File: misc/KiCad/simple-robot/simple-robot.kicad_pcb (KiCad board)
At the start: 2 copper layers, 99.8 x 81 mm, 44 parts, among them J1 MotLA, J10 Screw_Terminal_2_P5.00mm, J2 MotLB, J4 MotRA, J5 MotRB, J6 ENC_LF, J7 ENC_LR, J8 ENC_RF, J9 ENC_RR

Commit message: Update KiCad schematic to include all connections and IC
Make KiCad PCB 4-layer and update footprints
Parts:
- removed D3: LED_RAGB, common-hobby-things:LED RAGB
- removed R2, R3: 330k, Resistor_THT:R_Axial_DIN0207_L6.3mm_D2.5mm_P10.16mm_Horizontal
- added C19: 100nF_Ceramic, Capacitor_THT:C_Disc_D5.0mm_W2.5mm_P2.50mm, F.Cu at (-31.4, 168.1)
- added C20: 100nF_Ceramic, Capacitor_THT:C_Disc_D5.0mm_W2.5mm_P2.50mm, F.Cu at (40.8, 86.7)
- added C21: 100nF_Ceramic, Capacitor_THT:C_Disc_D5.0mm_W2.5mm_P2.50mm, F.Cu at (40.8, 90.8)
- added I1: ~, common-hobby-things:ICM-20948-module, F.Cu at (50.5, 86.8)
- added J11: JST02 HC-SR04, Connector_JST:JST_EH_B2B-EH-A_1x02_P2.50mm_Vertical, F.Cu at (-8.50, 162.2)
- added J3: JST03 Servo, Connector_JST:JST_EH_B3B-EH-A_1x03_P2.50mm_Vertical, F.Cu at (-8.50, 168.0)
- added LED1: LED_5mm_RGB_Kcom_RKGB, PCM_LED_THT_AKL:LED_D5.0mm-4_RGB_Wide_Pins, F.Cu at (88.1, 120.0)
- added R10: 220ohm, Resistor_THT:R_Axial_DIN0207_L6.3mm_D2.5mm_P10.16mm_Horizontal, F.Cu at (-10.4, 145.9)
- added R11: 220ohm, Resistor_THT:R_Axial_DIN0207_L6.3mm_D2.5mm_P10.16mm_Horizontal, F.Cu at (-10.4, 149.9)
- added R7: 20k, Resistor_THT:R_Axial_DIN0207_L6.3mm_D2.5mm_P10.16mm_Horizontal, F.Cu at (148.0, 61.5)
- added R8: 10k, Resistor_THT:R_Axial_DIN0207_L6.3mm_D2.5mm_P10.16mm_Horizontal, F.Cu at (152.3, 64.5)
- added R9: 330ohm, Resistor_THT:R_Axial_DIN0207_L6.3mm_D2.5mm_P10.16mm_Horizontal, F.Cu at (-10.4, 141.8)
- added SW1: RotaryEncoder_Switch, Rotary_Encoder:RotaryEncoder_Alps_EC11E-Switch_Vertical_H20mm, F.Cu at (98.2, 134.1)
- added U1: Pico2, PCM_SL_Development_Boards:raspberry_pi_pico_THT, F.Cu at (87.8, 64.8)
- added U2: CD4049UB, Package_DIP:DIP-16_W7.62mm_LongPads, F.Cu at (29.1, 86.7)
- moved B1 163.2 mm to (135.8, 64.7), turned to 180 degrees
- moved J10 131.5 mm to (147.8, 47.2), turned to 90 degrees
- moved C18 130.0 mm to (146.0, 74.2), turned to -90 degrees
- moved R4 121.3 mm to (152.3, 68.0), turned to 180 degrees
- moved MD1 117.2 mm to (113.1, 93.8), turned to 90 degrees
- moved C7 109.6 mm to (137.0, 70.8), turned to 90 degrees
- moved C1 102.0 mm to (137.2, 87.8), turned to 90 degrees
- moved MD2 98.7 mm to (113.1, 77.3), turned to 90 degrees
- moved R1 96.5 mm to (-80.8, 61.1)
- moved OLED1 93.8 mm to (68.5, 119.3)
- moved LS_1 87.3 mm to (65.1, 52.1)
- moved LS_2 87.0 mm to (79.5, 52.2)
- moved LS_3 86.9 mm to (93.9, 52.2)
- moved R6 25.6 mm to (34.9, 65.0)
- moved R5 16.9 mm to (35.2, 69.8)
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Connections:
- C14 pad 1: +5V -> +3V3
- LS_3 pad 1: unconnected-(LS_3-LV1-Pad1) -> US_SERVO
- LS_3 pad 11: unconnected-(LS_3-HV3-Pad11) -> Net-(LS_3-HV3)
- LS_3 pad 12: unconnected-(LS_3-HV4-Pad12) -> Net-(LS_3-HV4)
- LS_3 pad 3: unconnected-(LS_3-LV-Pad3) -> +3V3
- LS_3 pad 5: unconnected-(LS_3-LV3-Pad5) -> US_ECHO
- LS_3 pad 6: unconnected-(LS_3-LV4-Pad6) -> US_TRIG
- LS_3 pad 7: unconnected-(LS_3-HV1-Pad7) -> Net-(LS_3-HV1)
- LS_3 pad 9: unconnected-(LS_3-HV-Pad9) -> +5V
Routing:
- added copper zone on In2.Cu, net +3V3
- added copper zone on In1.Cu, net GND
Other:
- board size 99.8 x 81 mm -> 100 x 100 mm
- copper layers 2 -> 4
- board text added: "+"
- board text added: "-"
- board text added: "simple-robot 1-rafael-1 rev. 0.4 02/2026"

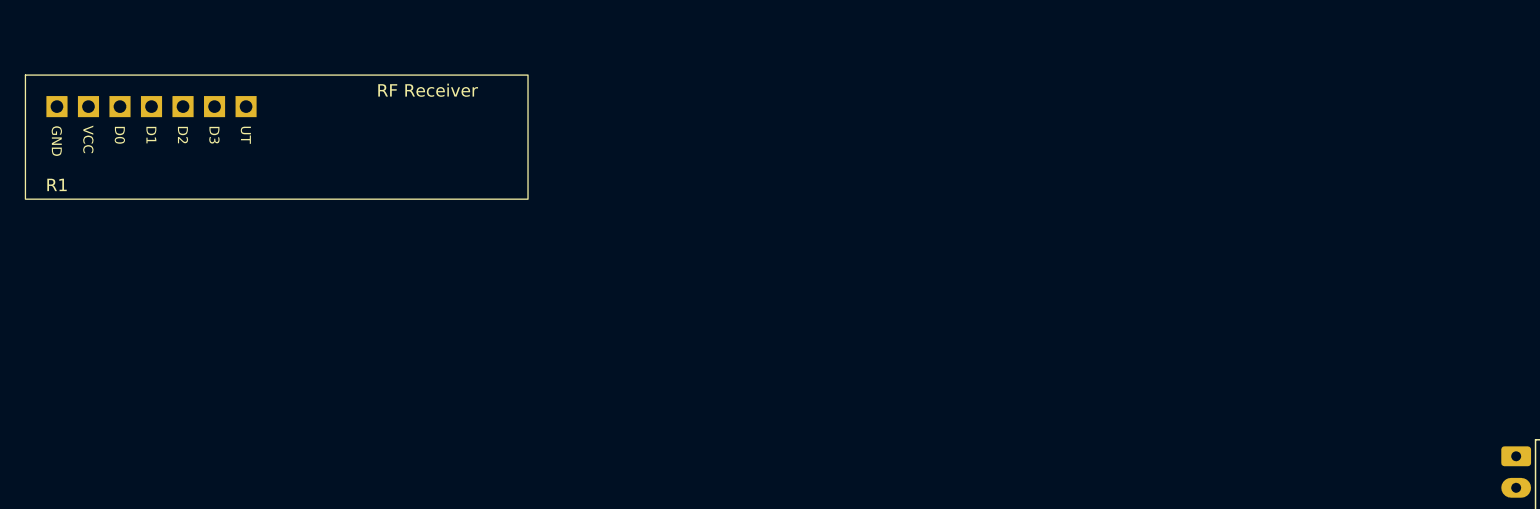
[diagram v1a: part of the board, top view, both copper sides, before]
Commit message: Add JST connectors, rename nets, update footprints
Rename power net +VBAT to +BATT and label several previously
unconnected nets (e.g. IR_OBST, GV_TX/GV_RX, Net-(D1-A), Net-(D3-A),
and various Jx pins). Add JST RF_PWR (J16) and RF_Logic (J15)
symbols to the schematic. Replace/adjust footprint and properties for
the capacitor/MD1 component and update reference/value/metadata.
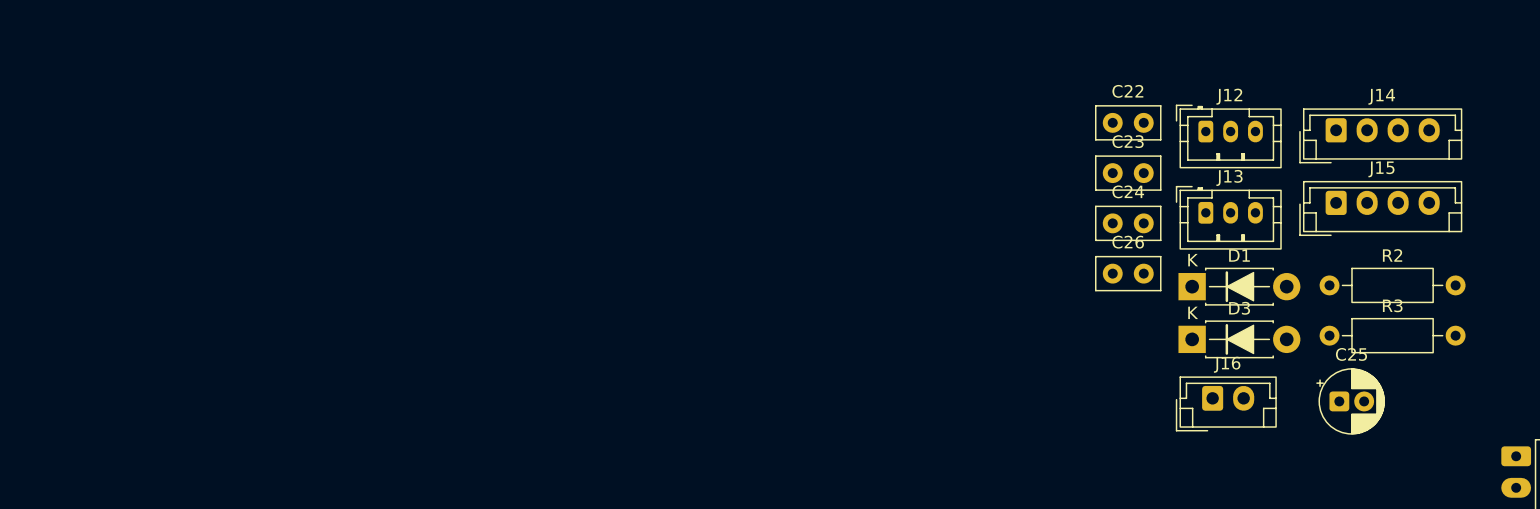
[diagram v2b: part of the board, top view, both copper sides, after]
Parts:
- removed R1: RF Receiver, common-hobby-things:433Mhz RC Receiver
- added C22: 100nF_Ceramic, Capacitor_THT:C_Disc_D5.0mm_W2.5mm_P2.50mm, F.Cu at (-3.38, 59.9)
- added C23: 100nF_Ceramic, Capacitor_THT:C_Disc_D5.0mm_W2.5mm_P2.50mm, F.Cu at (-3.38, 63.9)
- added C24: 100nF_Ceramic, Capacitor_THT:C_Disc_D5.0mm_W2.5mm_P2.50mm, F.Cu at (-3.38, 68.0)
- added C25: 10uF_16V, Capacitor_THT:CP_Radial_D5.0mm_P2.00mm, F.Cu at (14.9, 82.3)
- added C26: 100nF_Ceramic, Capacitor_THT:C_Disc_D5.0mm_W2.5mm_P2.50mm, F.Cu at (-3.38, 72.0)
- added D1: 1N5819, PCM_Diode_THT_AKL:D_DO-41_SOD81_P7.62mm_Horizontal, F.Cu at (3.02, 73.0)
- added D3: 1N5819, PCM_Diode_THT_AKL:D_DO-41_SOD81_P7.62mm_Horizontal, F.Cu at (3.02, 77.3)
- added J12: IR_RF, Connector_JST:JST_PH_B3B-PH-K_1x03_P2.00mm_Vertical, F.Cu at (4.12, 60.5)
- added J13: IR_LF, Connector_JST:JST_PH_B3B-PH-K_1x03_P2.00mm_Vertical, F.Cu at (4.12, 67.1)
- added J14: JST_GV, Connector_JST:JST_EH_B4B-EH-A_1x04_P2.50mm_Vertical, F.Cu at (14.6, 60.5)
- added J15: JST RF_Logic, Connector_JST:JST_EH_B4B-EH-A_1x04_P2.50mm_Vertical, F.Cu at (14.6, 66.3)
- added J16: JST RF_PWR, Connector_JST:JST_EH_B2B-EH-A_1x02_P2.50mm_Vertical, F.Cu at (4.67, 82.0)
- added R2: 47ohm, Resistor_THT:R_Axial_DIN0207_L6.3mm_D2.5mm_P10.16mm_Horizontal, F.Cu at (14.1, 73.0)
- added R3: 47ohm, Resistor_THT:R_Axial_DIN0207_L6.3mm_D2.5mm_P10.16mm_Horizontal, F.Cu at (14.1, 77.0)
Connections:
- net +VBAT renamed +BATT
- U1 pad 21: RESERVED_TX -> GV_RX
- U1 pad 22: RESERVED_RX -> GV_TX
- U2 pad 1: unconnected-(U2-Pad1) -> +3V3
- U2 pad 2: unconnected-(U2-Pad2) -> Net-(D1-A)
- U2 pad 3: unconnected-(U2-Pad3) -> Net-(J12-SIG)
- U2 pad 6: unconnected-(U2-Pad6) -> Net-(D3-A)
- U2 pad 7: unconnected-(U2-Pad7) -> Net-(J13-SIG)
- U2 pad 8: unconnected-(U2-Pad8) -> GND

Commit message: Update PCB layout: move footprints and pads
Update fp-info-cache (new hash) and add PCA9555 entry
Reposition many footprints and adjust silk text rotations/UUIDs
Change pad defaults (drill 2.8, width 3.2) and board prefs
(active layer and visible layers)
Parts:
- removed H3: MountingHole_Pad, MountingHole:MountingHole_3.7mm_Pad_Via
- added P1: Port Expander, common-hobby-things:PCA9555 Port Expander, F.Cu at (120.5, 142.2)
- moved H1 166.9 mm to (150.2, 115.3)
- moved C22 165.6 mm to (150.2, 121.8)
- moved C24 154.8 mm to (142.0, 121.0)
- moved D1 151.5 mm to (145.2, 125.2)
- moved C23 150.4 mm to (135.8, 121.0)
- moved J12 149.5 mm to (142.7, 116.8), turned to 90 degrees
- moved J13 141.4 mm to (136.5, 116.8), turned to 90 degrees
- moved D3 139.9 mm to (134.4, 125.2)
- moved U2 130.5 mm to (152.6, 129.0), turned to -90 degrees
- moved R11 111.1 mm to (97.0, 121.8)
- moved R9 109.9 mm to (96.9, 118.2)
- moved C9 103.3 mm to (106.5, 133.2), turned to -90 degrees
- moved R10 100.1 mm to (84.0, 112.7), turned to -90 degrees
- moved H2 90.6 mm to (60.7, 65.8)
- moved C6 67.1 mm to (64.8, 109.8)
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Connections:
- SW1 pad MP: (no net) -> GND
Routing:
- net +BATT: track 0.00 -> 116.6 mm
- net GND: track 0.00 -> 0.43 mm, vias 0 -> 36
- added copper zone on B.Cu, net GND
- added copper zone on F.Cu, net GND
- removed copper zone on In2.Cu, net +3V3
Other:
- board text added: "3V3"
- board text added: "GND"
- board text added: "L IR R"
- board text added: "Sig"

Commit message: Replace 2-pin JST with 4-pin and reposition parts
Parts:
- removed J11: JST02 HC-SR04, Connector_JST:JST_EH_B2B-EH-A_1x02_P2.50mm_Vertical
- J14 GV-AI: renamed from J14
- moved C26 152.9 mm to (147.2, 98.5), turned to -90 degrees
- moved J14 GV-AI 143.2 mm to (152.2, 100.0), turned to -90 degrees
- moved C25 128.2 mm to (142.0, 98.8), turned to -90 degrees
- moved R2 127.2 mm to (137.4, 104.2)
- moved R3 127.0 mm to (137.4, 107.2)
- moved J9EncRR 119.3 mm to (80.8, 72.8), turned to 180 degrees
- moved J7EncLR 113.5 mm to (75.5, 62.2), turned to -90 degrees
- moved C3 110.3 mm to (97.0, 60.2), turned to 90 degrees
- moved C14 109.2 mm to (91.0, 35.5), turned to 90 degrees
- moved J8EncRF 108.2 mm to (71.5, 72.8), turned to 180 degrees
- moved J6EncLF 104.2 mm to (68.2, 62.2), turned to -90 degrees
- moved C13 103.2 mm to (86.5, 35.5), turned to 90 degrees
- moved C10 90.1 mm to (82.2, 67.8), turned to 90 degrees
- moved J16-RFRCPW 87.8 mm to (89.5, 59.2)
- moved C17 85.5 mm to (84.2, 60.0), turned to 180 degrees
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- renumbered J15 to J15-RCRCVL, J16 to J16-RFRCPW, J3 to J3Servo, J6 to J6EncLF, J7 to J7EncLR, J8 to J8EncRF, J9 to J9EncRR
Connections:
- SW1 pad MP: GND -> (no net)
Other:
- board text added: "5V"
- board text added: "D0"
- board text added: "D1"
- board text added: "D2"
- board text added: "D3"
- board text added: "RX"
- board text added: "TX"

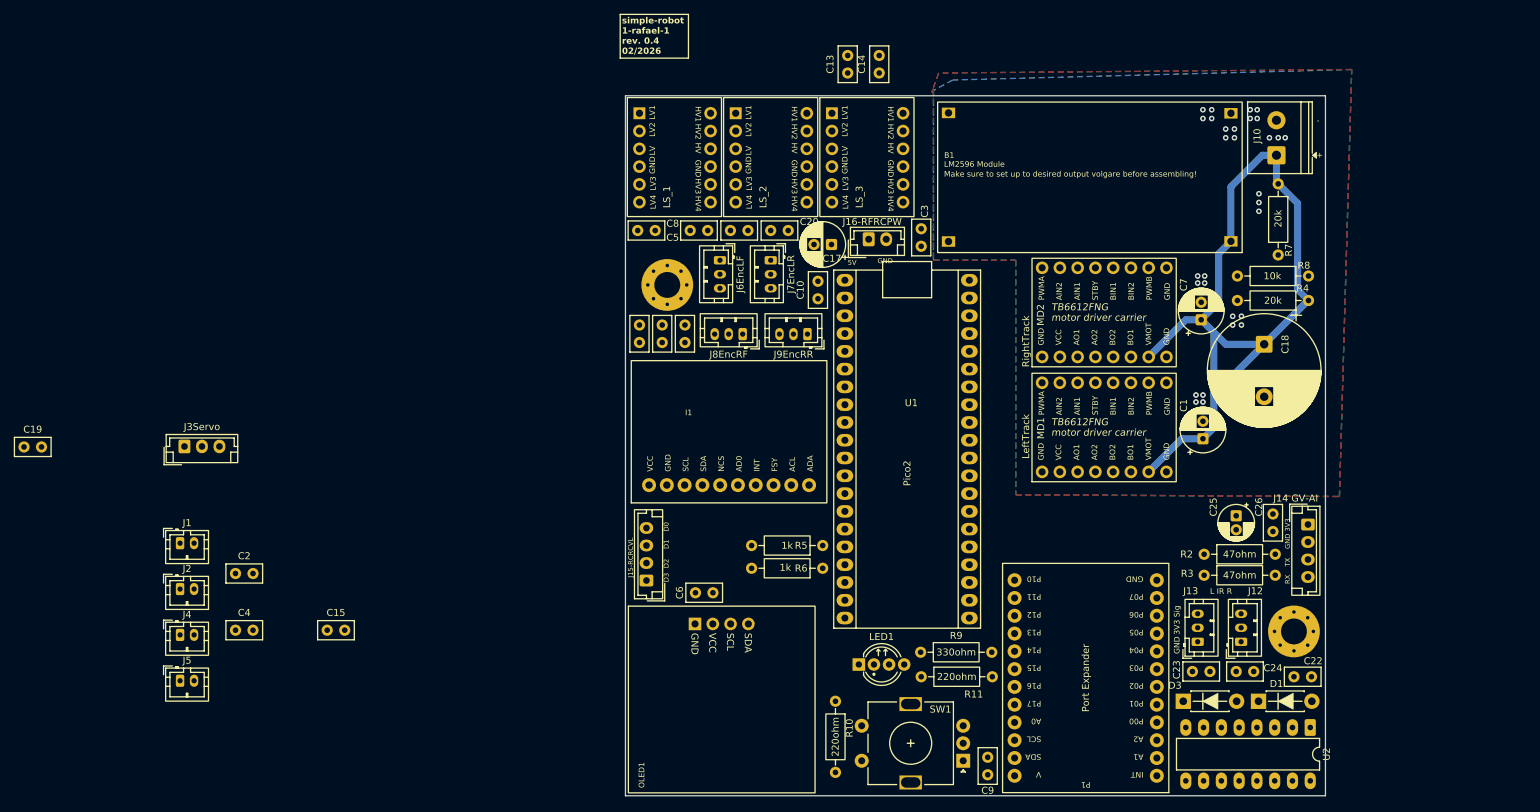
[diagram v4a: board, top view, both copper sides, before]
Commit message: pcb routing and some cleaning up; makingready for ordering the pcb mnufactured
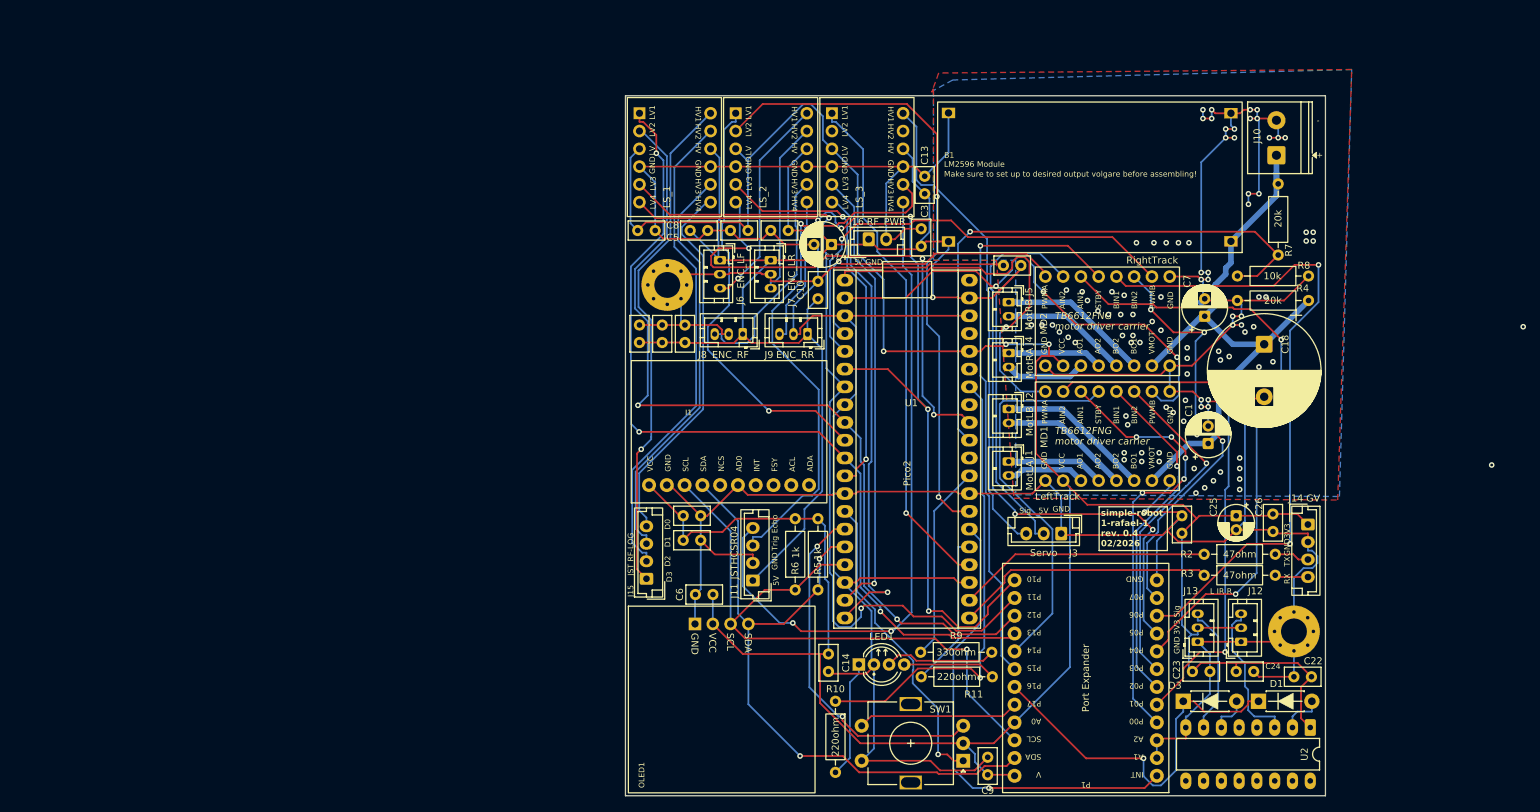
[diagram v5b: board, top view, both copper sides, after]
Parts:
- removed J3Servo: JST03 Servo, Connector_JST:JST_EH_B3B-EH-A_1x03_P2.50mm_Vertical
- added J11: JSTHCSR04, Connector_JST:JST_EH_B4B-EH-A_1x04_P2.50mm_Vertical, F.Cu at (73.0, 108.0)
- added J3: Servo, Connector_JST:JST_EH_B3B-EH-A_1x03_P2.50mm_Vertical, F.Cu at (117.0, 101.3)
- J14: renamed from J14 GV-AI; value JST_GV -> GV
- J15: renamed from J15-RCRCVL; value JST RF_Logic -> JST RF-LOG
- J16: renamed from J16-RFRCPW; value JST RF_PWR -> RF_PWR
- moved C19 165.9 mm to (134.2, 101.2), turned to 90 degrees
- moved J5 130.1 mm to (109.5, 68.2), turned to -90 degrees
- moved J4 125.0 mm to (109.5, 75.5), turned to -90 degrees
- moved J2 121.1 mm to (109.5, 83.5), turned to -90 degrees
- moved J1 118.9 mm to (109.5, 91.0), turned to -90 degrees
- moved C2 118.2 mm to (108.8, 63.0)
- moved C14 83.3 mm to (83.8, 118.5), turned to -90 degrees
- moved C4 66.0 mm to (63.0, 98.8)
- moved C15 52.5 mm to (63.0, 102.2)
- moved C13 20.5 mm to (97.5, 52.8)
- moved C5 7.50 mm to (64.0, 58.0)
- moved C8 7.50 mm to (56.5, 58.0)
- moved R5 6.36 mm to (82.2, 109.3), turned to 90 degrees
- moved R6 4.99 mm to (79.0, 109.3), turned to 90 degrees
- moved MD1 1.33 mm to (113.5, 95.0)
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- renumbered J6EncLF to J6, J7EncLR to J7, J8EncRF to J8, J9EncRR to J9
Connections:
- MD1 pad 5: Net-(J2-+) -> Net-(J2--)
- MD1 pad 6: Net-(J2--) -> Net-(J2-+)
- MD2 pad 5: Net-(J5-+) -> Net-(J5--)
- MD2 pad 6: Net-(J5--) -> Net-(J5-+)
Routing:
- net GND: track 0.43 -> 753.9 mm, vias 36 -> 102
- net +3V3: track 0.00 -> 400.4 mm, vias 0 -> 3
- net +5V: track 0.00 -> 244.0 mm, vias 0 -> 1
- net RC_A: track 0.00 -> 130.7 mm, vias 0 -> 5
- net RC_D: track 0.00 -> 125.6 mm, vias 0 -> 3
- net RC_C: track 0.00 -> 124.8 mm, vias 0 -> 2
- net RC_B: track 0.00 -> 121.1 mm, vias 0 -> 2
- net I2C SDA: track 0.00 -> 97.9 mm, vias 0 -> 2
- net Net-(LS_3-HV4): track 0.00 -> 95.9 mm, vias 0 -> 2
- net RMOT_R_FWD: track 0.00 -> 95.5 mm, vias 0 -> 2
- net I2C SCL: track 0.00 -> 93.5 mm, vias 0 -> 1
- net ENC_LR: track 0.00 -> 90.6 mm, vias 0 -> 2
- net RMOT_F_FWD: track 0.00 -> 86.7 mm, vias 0 -> 2
- net RMOT_F_REV: track 0.00 -> 86.1 mm, vias 0 -> 2
- net P_SENSE: track 0.00 -> 83.6 mm, vias 0 -> 1
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- added copper zone on In2.Cu, net +3V3
- added copper zone on In2.Cu, net +5V
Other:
- board text added: "Echo"
- board text added: "Trig"
